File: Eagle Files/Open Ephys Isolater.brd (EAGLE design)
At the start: 100 x 80 mm, 26 parts, among them J1 DC_POWER_JACK-PJ-102AH

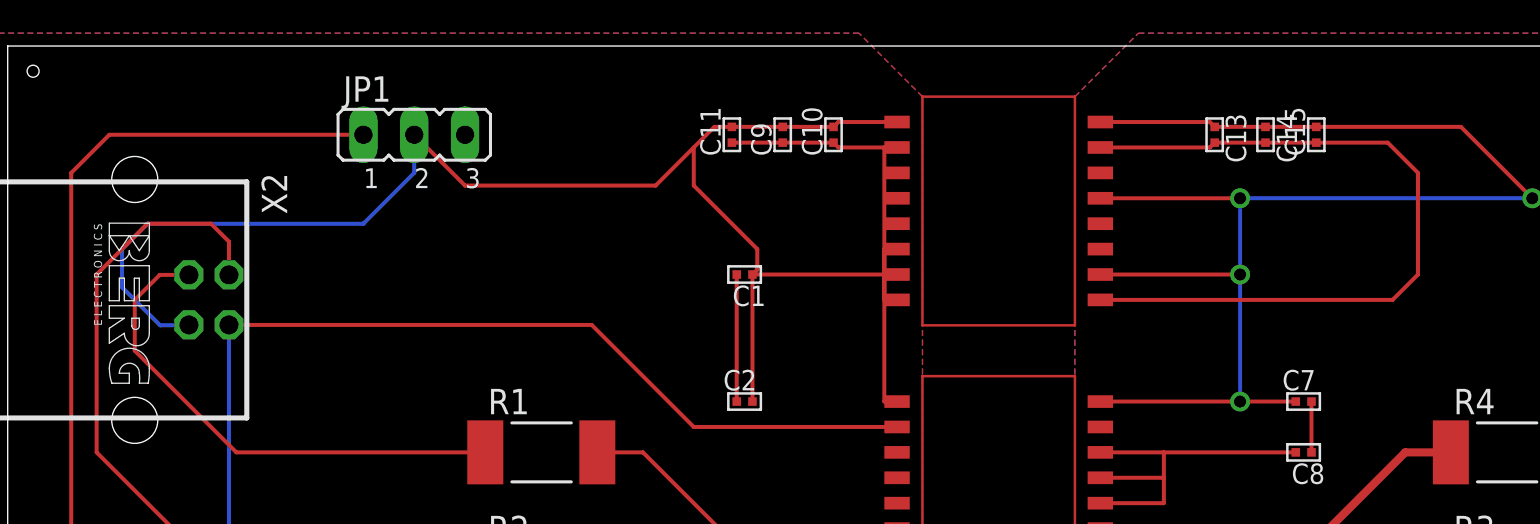
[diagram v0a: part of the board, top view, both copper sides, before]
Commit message: neatened nets on schematic
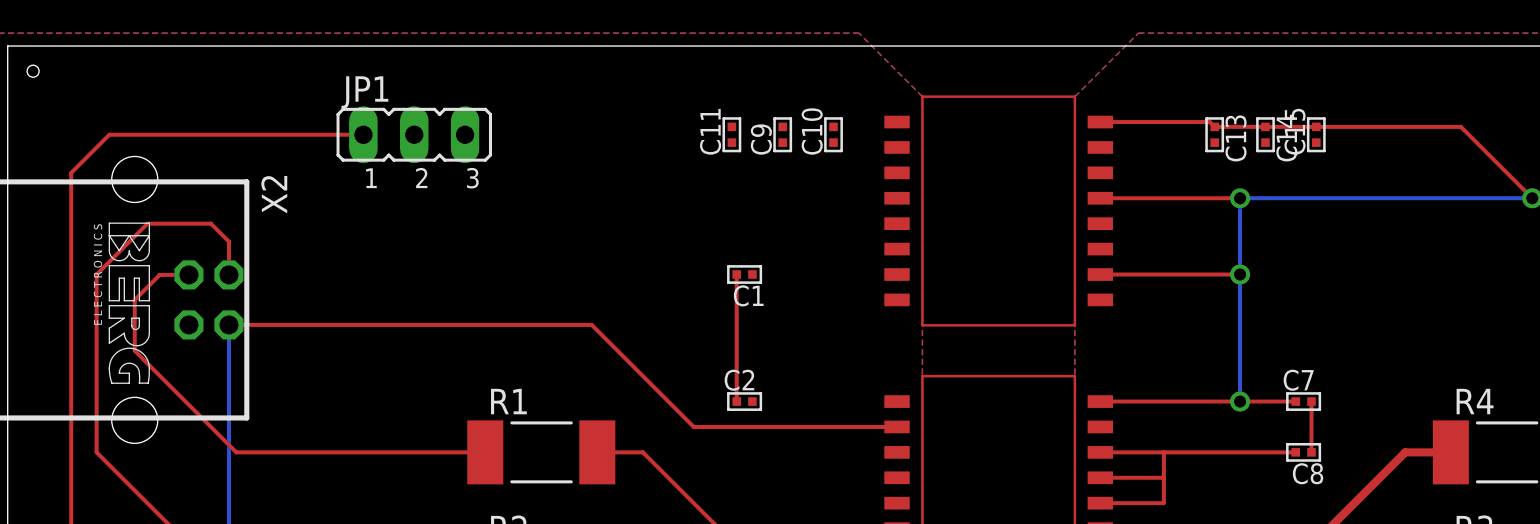
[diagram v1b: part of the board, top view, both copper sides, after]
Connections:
- net N$18 renamed V_ISO
- net N$4 renamed VDD1
- removed net N$16: C10.1, C11.1, C9.1, U$1.P$2, U$1.P$8
- net GND1: now also C10.1, C11.1, C9.1, U$1.P$2, U$1.P$8
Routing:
- net VDD1: track 80.9 -> 0.00 mm
- net N$2: track 38.1 -> 0.00 mm
- net N$16: track 16.6 -> 0.00 mm
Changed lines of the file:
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@@
 <?xml version="1.0" encoding="utf-8"?>
 <!DOCTYPE eagle SYSTEM "eagle.dtd">
-<eagle version="7.1.0">
+<eagle version="7.3.0">
 <drawing>
 <settings>
@@
 <wire x1="26.67" y1="45.72" x2="39.37" y2="45.72" width="0.2" layer="1"/>
 </signal>
-<signal name="N$2">
-<contactref element="U$1" pad="P$10"/>
-<contactref element="C13" pad="2"/>
-<contactref element="C14" pad="2"/>
-<contactref element="C15" pad="1"/>
-<contactref element="U$1" pad="P$16"/>
-<wire x1="54.61" y1="74.93" x2="60.0837" y2="74.93" width="0.2" layer="1"/>
-<wire x1="60.0837" y1="74.93" x2="60.325" y2="75.1713" width="0.2" layer="1"/>
-<wire x1="60.325" y1="75.1713" x2="62.865" y2="75.1713" width="0.2" layer="1"/>
-<wire x1="62.865" y1="75.1713" x2="65.405" y2="75.1713" width="0.2" layer="1"/>
-<wire x1="54.61" y1="67.31" x2="69.215" y2="67.31" width="0.2" layer="1"/>
-<wire x1="69.215" y1="67.31" x2="70.485" y2="68.58" width="0.2" layer="1"/>
-<wire x1="65.405" y1="75.1713" x2="68.9737" y2="75.1713" width="0.2" layer="1"/>
-<wire x1="68.9737" y1="75.1713" x2="70.485" y2="73.66" width="0.2" layer="1"/>
-<wire x1="70.485" y1="73.66" x2="70.485" y2="68.58" width="0.2" layer="1"/>
-</signal>
-<signal name="N$16">
-<contactref element="C10" pad="1"/>
-<contactref element="C9" pad="1"/>
-<contactref element="C11" pad="1"/>
-<contactref element="U$1" pad="P$8"/>
-<contactref element="U$1" pad="P$2"/>
-<wire x1="44.45" y1="74.93" x2="43.815" y2="74.93" width="0.2" layer="1"/>
-<wire x1="43.815" y1="74.93" x2="41.5163" y2="74.93" width="0.2" layer="1"/>
-<wire x1="41.5163" y1="74.93" x2="41.275" y2="75.1713" width="0.2" layer="1"/>
-<wire x1="41.275" y1="75.1713" x2="38.735" y2="75.1713" width="0.2" layer="1"/>
-<wire x1="38.735" y1="75.1713" x2="36.195" y2="75.1713" width="0.2" layer="1"/>
-<wire x1="44.45" y1="67.31" x2="43.815" y2="67.31" width="0.2" layer="1"/>
-<wire x1="43.815" y1="74.93" x2="43.815" y2="67.31" width="0.2" layer="1"/>
-</signal>
-<signal name="N$18">
+<signal name="V_ISO">
 <contactref element="U$2" pad="P$9"/>
 <contactref element="C7" pad="1"/>
@@
 <wire x1="29.19" y1="66.06" x2="34.29" y2="60.96" width="0.2" layer="1"/>
 <wire x1="34.29" y1="60.96" x2="44.45" y2="60.96" width="0.2" layer="1"/>
-<wire x1="44.45" y1="60.96" x2="44.45" y2="53.34" width="0" layer="19" extent="1-1"/>
 <wire x1="11.06" y1="66.06" x2="11.06" y2="52.795" width="0.2" layer="16"/>
 <wire x1="11.06" y1="52.795" x2="3.985" y2="45.72" width="0.2" layer="16"/>
-</signal>
-<signal name="N$4">
-<contactref element="C2" pad="2"/>
-<contactref element="U$2" pad="P$3"/>
-<contactref element="U$2" pad="P$5"/>
-<contactref element="U$2" pad="P$1"/>
-<contactref element="C1" pad="1"/>
-<contactref element="C9" pad="2"/>
-<contactref element="C11" pad="2"/>
-<contactref element="X2" pad="4"/>
-<contactref element="U$1" pad="P$6"/>
-<contactref element="C10" pad="2"/>
-<contactref element="U$1" pad="P$1"/>
-<contactref element="U$1" pad="P$7"/>
-<contactref element="U$2" pad="P$4"/>
-<contactref element="JP1" pad="2"/>
-<wire x1="44.45" y1="76.2" x2="41.5163" y2="76.2" width="0.2" layer="1"/>
-<wire x1="41.5163" y1="76.2" x2="41.275" y2="75.9587" width="0.2" layer="1"/>
-<wire x1="41.275" y1="75.9587" x2="38.735" y2="75.9587" width="0.2" layer="1"/>
-<wire x1="38.735" y1="75.9587" x2="36.195" y2="75.9587" width="0.2" layer="1"/>
-<wire x1="36.195" y1="75.9587" x2="35.3187" y2="75.9587" width="0.2" layer="1"/>
-<wire x1="35.3187" y1="75.9587" x2="34.29" y2="74.93" width="0.2" layer="1"/>
-<wire x1="37.2237" y1="68.58" x2="43.815" y2="68.58" width="0.2" layer="1"/>
-<wire x1="44.45" y1="69.85" x2="43.815" y2="69.85" width="0.2" layer="1"/>
-<wire x1="43.815" y1="69.85" x2="43.815" y2="68.58" width="0.2" layer="1"/>
-<wire x1="34.29" y1="74.93" x2="34.29" y2="73.025" width="0.2" layer="1"/>
-<wire x1="34.29" y1="73.025" x2="37.465" y2="69.85" width="0.2" layer="1"/>
-<wire x1="37.465" y1="69.85" x2="37.465" y2="68.8213" width="0.2" layer="1"/>
-<wire x1="37.465" y1="68.8213" x2="37.2237" y2="68.58" width="0.2" layer="1"/>
-<wire x1="37.2237" y1="68.58" x2="37.2237" y2="62.23" width="0.2" layer="1"/>
-<wire x1="44.45" y1="68.58" x2="43.815" y2="68.58" width="0.2" layer="1"/>
-<wire x1="43.815" y1="68.58" x2="43.815" y2="62.23" width="0.2" layer="1"/>
-<wire x1="43.815" y1="62.23" x2="44.45" y2="62.23" width="0.2" layer="1"/>
-<wire x1="20.32" y1="75.565" x2="20.32" y2="73.66" width="0.2" layer="16"/>
-<wire x1="20.32" y1="73.66" x2="17.78" y2="71.12" width="0.2" layer="16"/>
-<wire x1="17.78" y1="71.12" x2="6.985" y2="71.12" width="0.2" layer="16"/>
-<wire x1="6.985" y1="71.12" x2="5.715" y2="69.85" width="0.2" layer="16"/>
-<wire x1="5.715" y1="69.85" x2="5.715" y2="67.945" width="0.2" layer="16"/>
-<wire x1="5.715" y1="67.945" x2="7.62" y2="66.04" width="0.2" layer="16"/>
-<wire x1="7.62" y1="66.04" x2="9.04" y2="66.04" width="0.2" layer="16"/>
-<wire x1="9.04" y1="66.04" x2="9.06" y2="66.06" width="0.2" layer="16"/>
-<wire x1="44.45" y1="58.42" x2="44.45" y2="59.69" width="0" layer="19" extent="1-1"/>
-<wire x1="44.45" y1="57.15" x2="44.45" y2="58.42" width="0" layer="19" extent="1-1"/>
-<wire x1="44.45" y1="62.23" x2="44.45" y2="59.69" width="0" layer="19" extent="1-1"/>
-<wire x1="34.29" y1="74.93" x2="32.385" y2="73.025" width="0.2" layer="1"/>
-<wire x1="32.385" y1="73.025" x2="22.86" y2="73.025" width="0.2" layer="1"/>
-<wire x1="22.86" y1="73.025" x2="20.32" y2="75.565" width="0.2" layer="1"/>
+<contactref element="C9" pad="1"/>
+<contactref element="C10" pad="1"/>
+<contactref element="C11" pad="1"/>
+<contactref element="U$1" pad="P$2"/>
+<contactref element="U$1" pad="P$8"/>
+<wire x1="41.275" y1="75.1713" x2="44.45" y2="74.93" width="0" layer="19" extent="1-1"/>
+<wire x1="38.735" y1="75.1713" x2="41.275" y2="75.1713" width="0" layer="19" extent="1-1"/>
+<wire x1="36.195" y1="75.1713" x2="38.735" y2="75.1713" width="0" layer="19" extent="1-1"/>
+<wire x1="44.45" y1="67.31" x2="44.45" y2="74.93" width="0" layer="19" extent="1-1"/>
+<wire x1="44.45" y1="60.96" x2="44.45" y2="67.31" width="0" layer="19" extent="1-1"/>
+<wire x1="44.45" y1="53.34" x2="44.45" y2="60.96" width="0" layer="19" extent="1-1"/>
 </signal>
 <signal name="N$1">
@@
 <wire x1="78.105" y1="38.58" x2="81.28" y2="38.58" width="0.2" layer="16"/>
 </signal>
+<signal name="VDD1">
+<contactref element="U$1" pad="P$7"/>
+<contactref element="X2" pad="4"/>
+<contactref element="U$1" pad="P$6"/>
+<contactref element="C10" pad="2"/>
+<contactref element="C9" pad="2"/>
+<contactref element="C11" pad="2"/>
+<contactref element="JP1" pad="2"/>
+<contactref element="U$1" pad="P$1"/>
+<contactref element="C1" pad="1"/>
+<contactref element="U$2" pad="P$1"/>
+<contactref element="C2" pad="2"/>
+<contactref element="U$2" pad="P$4"/>
+<contactref element="U$2" pad="P$3"/>
+<contactref element="U$2" pad="P$5"/>
+<wire x1="41.275" y1="75.9587" x2="44.45" y2="76.2" width="0" layer="19" extent="1-1"/>
+<wire x1="38.735" y1="75.9587" x2="41.275" y2="75.9587" width="0" layer="19" extent="1-1"/>
+<wire x1="36.195" y1="75.9587" x2="38.735" y2="75.9587" width="0" layer="19" extent="1-1"/>
+<wire x1="44.45" y1="69.85" x2="44.45" y2="76.2" width="0" layer="19" extent="1-1"/>
+<wire x1="44.45" y1="68.58" x2="44.45" y2="69.85" width="0" layer="19" extent="1-1"/>
+<wire x1="44.45" y1="62.23" x2="44.45" y2="68.58" width="0" layer="19" extent="1-1"/>
+<wire x1="44.45" y1="59.69" x2="44.45" y2="62.23" width="0" layer="19" extent="1-1"/>
+<wire x1="44.45" y1="58.42" x2="44.45" y2="59.69" width="0" layer="19" extent="1-1"/>
+<wire x1="44.45" y1="57.15" x2="44.45" y2="58.42" width="0" layer="19" extent="1-1"/>
+<wire x1="37.2237" y1="68.58" x2="44.45" y2="68.58" width="0" layer="19" extent="1-1"/>
+<wire x1="37.2237" y1="62.23" x2="37.2237" y2="68.58" width="0" layer="19" extent="1-1"/>
+<wire x1="20.32" y1="75.565" x2="36.195" y2="75.9587" width="0" layer="19" extent="1-1"/>
+<wire x1="9.06" y1="66.06" x2="20.32" y2="75.565" width="0" layer="19" extent="1-1"/>
+</signal>
+<signal name="N$2">
+<contactref element="C15" pad="1"/>
+<contactref element="C13" pad="2"/>
+<contactref element="C14" pad="2"/>
+<contactref element="U$1" pad="P$16"/>
+<contactref element="U$1" pad="P$10"/>
+<wire x1="62.865" y1="75.1713" x2="65.405" y2="75.1713" width="0" layer="19" extent="1-1"/>
+<wire x1="60.325" y1="75.1713" x2="62.865" y2="75.1713" width="0" layer="19" extent="1-1"/>
+<wire x1="54.61" y1="74.93" x2="60.325" y2="75.1713" width="0" layer="19" extent="1-1"/>
+<wire x1="54.61" y1="67.31" x2="54.61" y2="74.93" width="0" layer="19" extent="1-1"/>
+</signal>
 </signals>

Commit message: more names, labels, neatening
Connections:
- removed net N$2: C13.2, C14.2, C15.1, U$1.P$10, U$1.P$16
- net GND2: now also C13.2, C14.2, C15.1, U$1.P$10, U$1.P$16
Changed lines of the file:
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@@
 <vertex x="55.88" y="3.81"/>
 </polygon>
+<contactref element="C15" pad="1"/>
+<contactref element="C13" pad="2"/>
+<contactref element="C14" pad="2"/>
+<contactref element="U$1" pad="P$16"/>
+<contactref element="U$1" pad="P$10"/>
+<wire x1="65.405" y1="75.1713" x2="91.27" y2="70.81" width="0" layer="19" extent="1-1"/>
+<wire x1="62.865" y1="75.1713" x2="65.405" y2="75.1713" width="0" layer="19" extent="1-1"/>
+<wire x1="60.325" y1="75.1713" x2="62.865" y2="75.1713" width="0" layer="19" extent="1-1"/>
+<wire x1="54.61" y1="74.93" x2="60.325" y2="75.1713" width="0" layer="19" extent="1-1"/>
+<wire x1="54.61" y1="67.31" x2="54.61" y2="74.93" width="0" layer="19" extent="1-1"/>
+<wire x1="54.61" y1="60.96" x2="54.61" y2="67.31" width="0" layer="19" extent="1-1"/>
+<wire x1="54.61" y1="53.34" x2="54.61" y2="60.96" width="0" layer="19" extent="1-1"/>
+<wire x1="60.96" y1="25.4" x2="57.15" y2="45.72" width="0" layer="19" extent="1-1"/>
 </signal>
 <signal name="N$21">
@@
 <wire x1="9.06" y1="66.06" x2="20.32" y2="75.565" width="0" layer="19" extent="1-1"/>
 </signal>
-<signal name="N$2">
-<contactref element="C15" pad="1"/>
-<contactref element="C13" pad="2"/>
-<contactref element="C14" pad="2"/>
-<contactref element="U$1" pad="P$16"/>
-<contactref element="U$1" pad="P$10"/>
-<wire x1="62.865" y1="75.1713" x2="65.405" y2="75.1713" width="0" layer="19" extent="1-1"/>
-<wire x1="60.325" y1="75.1713" x2="62.865" y2="75.1713" width="0" layer="19" extent="1-1"/>
-<wire x1="54.61" y1="74.93" x2="60.325" y2="75.1713" width="0" layer="19" extent="1-1"/>
-<wire x1="54.61" y1="67.31" x2="54.61" y2="74.93" width="0" layer="19" extent="1-1"/>
-</signal>
 </signals>
